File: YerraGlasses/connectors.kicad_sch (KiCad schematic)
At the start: 4 parts, among them J1 Conn_01x02_Pin, J2 Conn_01x02_Pin, J3 Conn_01x02_Pin, J4 Conn_01x02_Pin

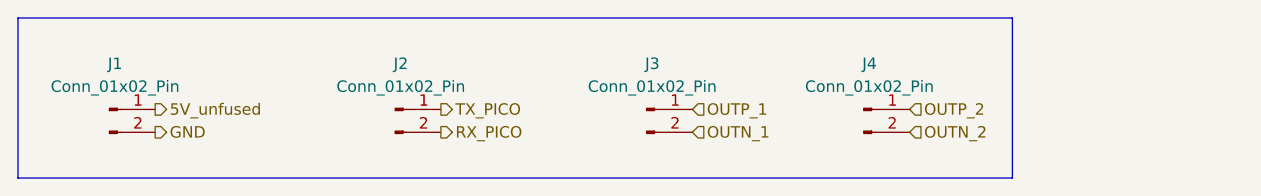
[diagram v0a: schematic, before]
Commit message: added power connector, updated cad
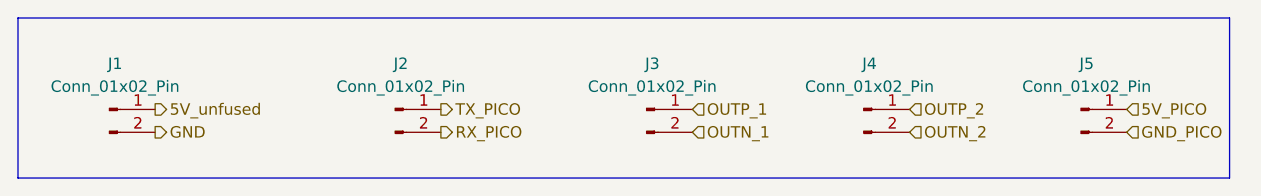
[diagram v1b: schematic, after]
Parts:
- added J5: Conn_01x02_Pin, Connector_JST:JST_EH_B2B-EH-A_1x02_P2.50mm_Vertical, symbol Connector:Conn_01x02_Pin
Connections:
- new net 5V_PICO: J5.1 (Pin_1)
- new net GND_PICO: J5.2 (Pin_2)
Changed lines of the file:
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@@
 	(polyline
 		(pts
-			(xy 125.73 13.97) (xy 125.73 31.75)
+			(xy 149.86 13.97) (xy 149.86 31.75)
 		)
 		(stroke
@@
 	(polyline
 		(pts
-			(xy 15.24 13.97) (xy 125.73 13.97)
+			(xy 15.24 13.97) (xy 149.86 13.97)
 		)
 		(stroke
@@
 	(polyline
 		(pts
-			(xy 125.73 31.75) (xy 15.24 31.75)
+			(xy 149.86 31.75) (xy 15.24 31.75)
 		)
 		(stroke
@@
 			(font
 				(size 1.27 1.27)
+			)
+			(justify left)
+		)
+	)
+	(hierarchical_label "5V_PICO"
+		(shape input)
+		(at 138.43 24.13 0)
+		(effects
+			(font
+				(size 1.27 1.27)
+			)
+			(justify left)
+		)
+	)
+	(hierarchical_label "GND_PICO"
+		(shape input)
+		(at 138.43 26.67 0)
+		(effects
+			(font
+				(size 1.27 1.27)
+				(thickness 0.1588)
 			)
 			(justify left)
@@
 					(unit 1)
 				)
+			)
+		)
+	)
+	(symbol
+		(lib_id "Connector:Conn_01x02_Pin")
+		(at 133.35 24.13 0)
+		(unit 1)
+		(exclude_from_sim no)
+		(in_bom yes)
+		(on_board yes)
+		(dnp no)
+		(fields_autoplaced yes)
+		(property "Reference" "J5"
+			(at 133.985 19.05 0)
+			(effects
+				(font
+					(size 1.27 1.27)
+				)
+			)
+		)
+		(property "Value" "Conn_01x02_Pin"
+			(at 133.985 21.59 0)
+			(effects
+				(font
+					(size 1.27 1.27)
+				)
+			)
+		)
+		(property "Footprint" "Connector_JST:JST_EH_B2B-EH-A_1x02_P2.50mm_Vertical"
+			(at 133.35 24.13 0)
+			(effects
+				(font
+					(size 1.27 1.27)
+				)
+				(hide yes)
+			)
+		)
+		(property "Datasheet" "~"
+			(at 133.35 24.13 0)
+			(effects
+				(font
+					(size 1.27 1.27)
+				)
+				(hide yes)
+			)
+		)
+		(property "Description" "Generic connector, single row, 01x02, script generated"
+			(at 133.35 24.13 0)
+			(effects
+				(font
+					(size 1.27 1.27)
+				)
+				(hide yes)
+			)
+		)
+		(pin "2"
+		)
+		(pin "1"
+		)
+		(instances
+			(project "YerraGlasses"
+				(path "/565dd4cd-3458-4e26-8cb8-cc6b370af252/5390385b-9d52-4962-9ccb-8c4e0a3e3df7"
+					(reference "J5")
+					(unit 1)
+				)
